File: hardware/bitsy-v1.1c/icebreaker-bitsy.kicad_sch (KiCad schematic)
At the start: 99 parts, among them J1 USB_C, P0 0, P1 1, P10 10, P11 11, P12 12, P13 13, P14 14, P15 15, P16 16, P17 17, P18 18, P19 19, P2 2, P20 20, P21 21, P22 22, P23 23, P24 GND, P25 GND, P26 GND, P27 3V3, P28 3V3, P29 VIN, P3 3, P30 CDONE, P31 CRESET, P32 UP, P33 UP, P34 UP, P35 UP, P36 CS, P37 SCK, P38 CIPO, P39 COPI, P4 4, P40 IO3, P41 IO2, P5 5, P6 6, P7 7, P8 8, P9 9, SW1 TACT, U1 USBLC6-2, U2 TLV75533PDRV, U3 TLV73312PDRV, U4 LY68L6400, U5 W25Q128JVxxM, U6 ICE40UP5K-SG48, X1 12MHz

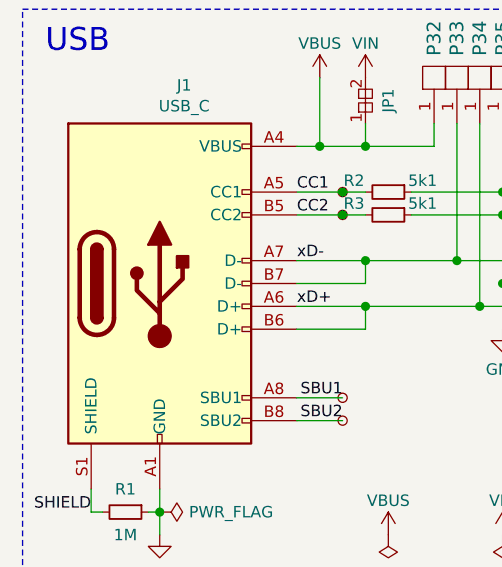
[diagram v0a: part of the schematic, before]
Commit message: Updated all design files to KiCad V8.0.6.
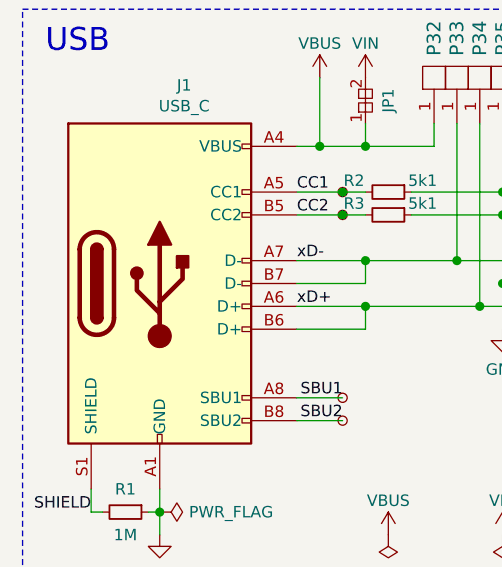
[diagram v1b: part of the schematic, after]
